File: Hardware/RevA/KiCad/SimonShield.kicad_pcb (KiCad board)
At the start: 2 copper layers, 68.6 x 53.3 mm, 37 parts, among them J1 ARDUINO, SW0 LED_KEY, SW1 LED_KEY, SW2 LED_KEY, SW3 LED_KEY

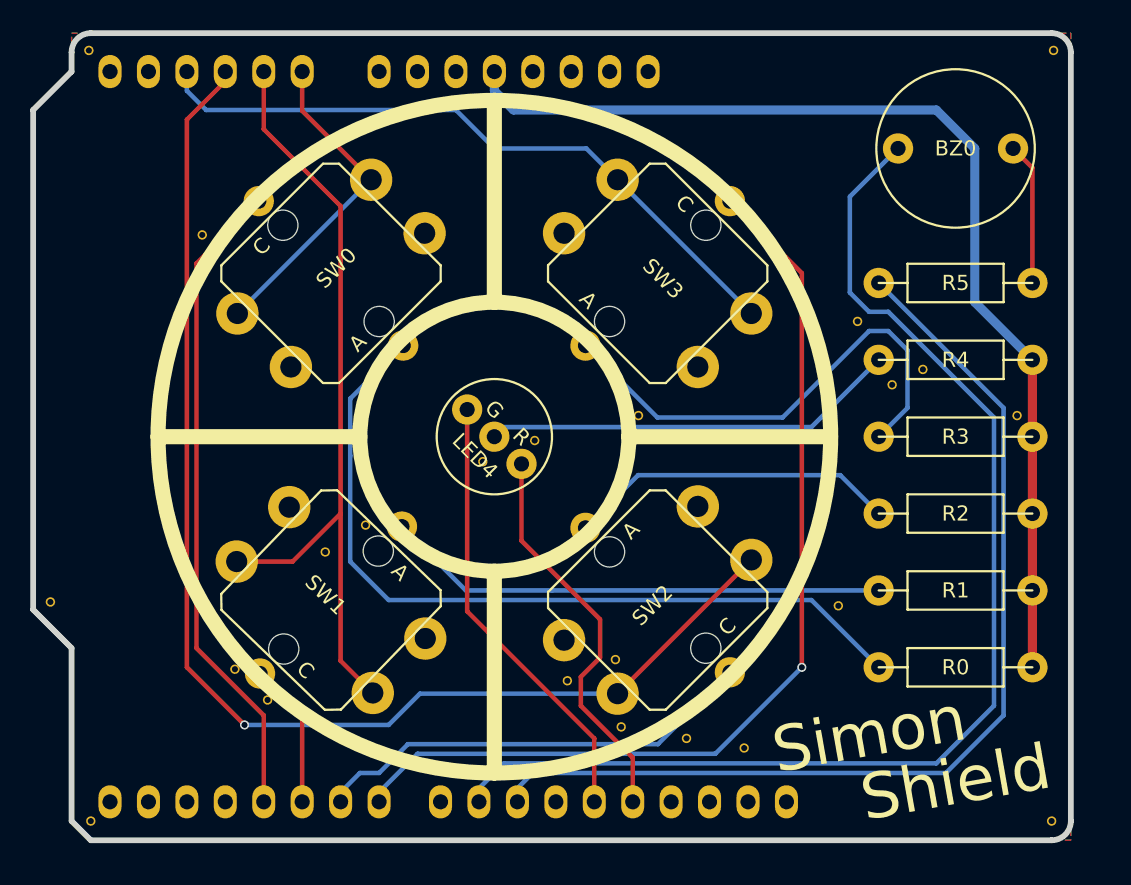
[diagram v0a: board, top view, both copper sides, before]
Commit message: modified PCB layout
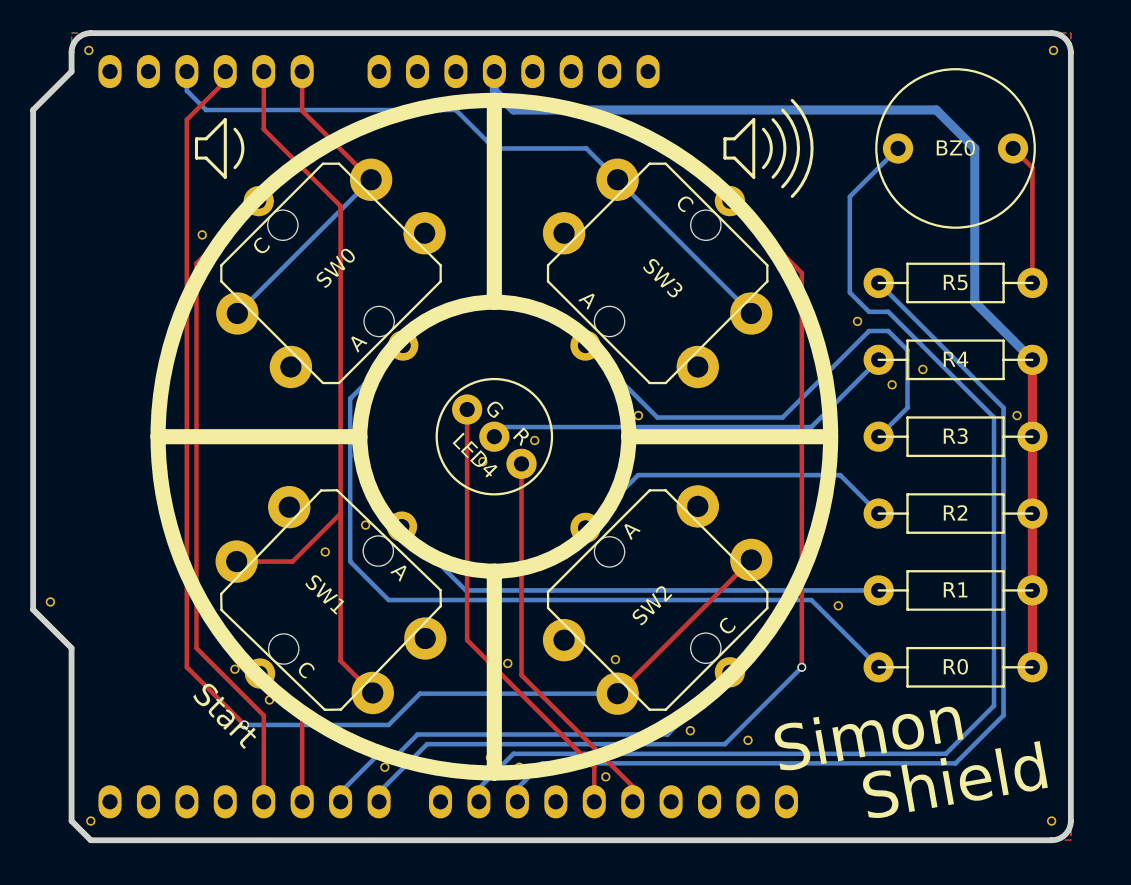
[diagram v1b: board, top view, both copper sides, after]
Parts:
- added VIA: GND, via, F.Cu at (147.7, 127.3)
- added VIA: GND, via, F.Cu at (138.8, 127.3)
- added VIA: GND, via, F.Cu at (145.8, 126.6)
- moved VIA 4.10 mm to (146.9, 120.4)
- moved VIA 3.45 mm to (153.4, 127.9)
- moved VIA 0.57 mm to (159.0, 124.8)
- moved VIA 0.57 mm to (162.8, 125.5)
- moved VIA 0.13 mm to (131.2, 122.8)
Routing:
- net /LED4_R: track 26.4 -> 25.4 mm
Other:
- board text added: "Start"
- board text added: "https://hotwolf.github.io/SimonShield"
